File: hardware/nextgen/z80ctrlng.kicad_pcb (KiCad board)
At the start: 4 copper layers, 101.6 x 53.3 mm, 67 parts, among them J1 RCBUS, J11 U254-051T-4BH81-S2S, J3 UDPI, J5 XKTF-0803-0, J6 UEXT, J9 SM04B-SRSS-TB, Q3 BSS138, SW1 RESET, SW2 BANK_EN, SW4 PROG_EN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

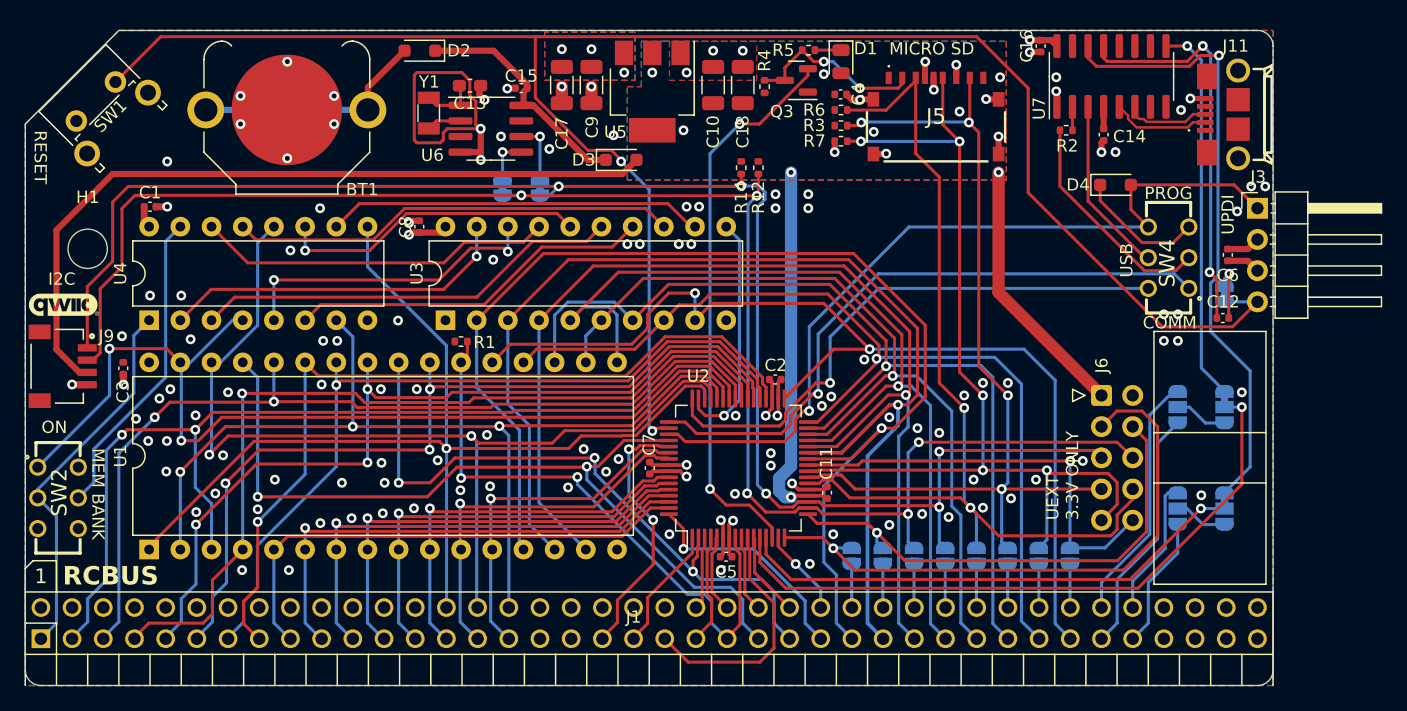
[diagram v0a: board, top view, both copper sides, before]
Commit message: Reorganize hardware directories
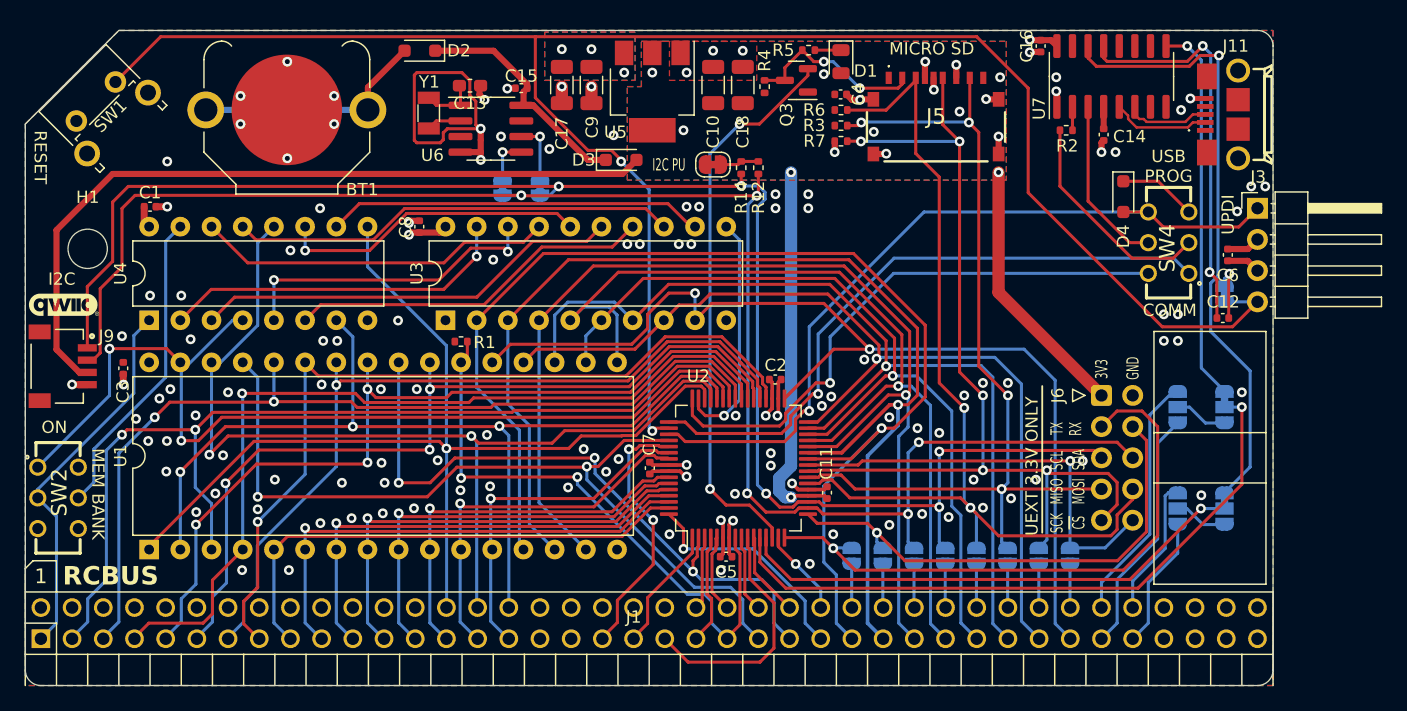
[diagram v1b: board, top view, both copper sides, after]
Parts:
- added JP16: I2C_PU, Jumper:SolderJumper-2_P1.3mm_Bridged_RoundedPad1.0x1.5mm, F.Cu at (183.8, 84.3)
- moved SW4 1.22 mm to (220.9, 90.7)
- moved D4 1.15 mm to (217.2, 86.9), turned to -90 degrees
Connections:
- R12 pad 1: +3.3V -> Net-(JP16-A)
- R14 pad 1: +3.3V -> Net-(JP16-A)
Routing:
- net Net-(D4-K): track 10.4 -> 6.37 mm
- net Net-(JP16-A): track 0.00 -> 3.15 mm
- net UPDI: track 66.2 -> 63.6 mm
- net RXF: track 51.8 -> 52.4 mm
- net /Peripherals/USBRX: track 14.5 -> 14.0 mm
- net TXF: track 46.0 -> 46.5 mm
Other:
- board text added: "3V3"
- board text added: "GND"
- board text added: "I2C PU"
- board text added: "USB PROG"
- board text removed: "PROG"
- board text removed: "USB"

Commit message: Get rid of serial bus links, make banking software controllable
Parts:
- removed JP12: RXB, Jumper:SolderJumper-3_P1.3mm_Open_RoundedPad1.0x1.5mm
- removed JP14: CTS, Jumper:SolderJumper-3_P1.3mm_Bridged12_RoundedPad1.0x1.5mm
- removed JP4: TXB, Jumper:SolderJumper-3_P1.3mm_Open_RoundedPad1.0x1.5mm
- removed JP5: RTS, Jumper:SolderJumper-3_P1.3mm_Bridged12_RoundedPad1.0x1.5mm
- removed SW2: BANK_EN, SamacSys_Parts:JS202011CQN
- added C19: 0.1uf, Capacitor_SMD:C_0402_1005Metric, F.Cu at (130.3, 110.0)
- added U8: 74LVC1G126, Package_TO_SOT_SMD:SOT-353_SC-70-5, F.Cu at (130.5, 112.2)
- U3: value 74HCT574 -> 74HCT573; footprint Package_DIP:DIP-20_W7.62mm -> Package_SO:TSSOP-20_4.4x6.5mm_P0.65mm
- U4: footprint Package_DIP:DIP-16_W7.62mm -> Package_SO:SOIC-16_3.9x9.9mm_P1.27mm
- moved U3 15.2 mm to (176.3, 92.1)
- moved C8 12.4 mm to (172.2, 89.3)
- moved U4 6.01 mm to (141.6, 92.3)
- moved C3 4.87 mm to (137.9, 96.6), turned to 0 degrees
- moved U1 2.23 mm to (137.9, 113.4)
- moved R1 2.22 mm to (163.3, 96.5)
- moved JP15 0.97 mm to (165.9, 85.6)
- moved JP13 0.71 mm to (169.3, 85.6)
- moved JP16 0.34 mm to (183.5, 84.1)
- moved C1 0.31 mm to (137.6, 87.8)
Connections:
- U2 pad 1: /~{Z80RST} -> /~{BUSACK}
- U2 pad 12: TXB -> /~{Z80RST}
- U2 pad 13: RXB -> /~{INT}
- U2 pad 14: ~{SDCS} -> /~{RD}
- U2 pad 2: /~{RD} -> /~{HALT}
- U2 pad 3: /~{BUSACK} -> /A16
- U2 pad 4: /~{INT} -> /A17
- U2 pad 44: /A16 -> /~{BANK}
- U2 pad 45: /A17 -> /BLAT
- U2 pad 46: /A18 -> ~{SDCS}
- U2 pad 47: /BCK -> ~{CTS}
- U2 pad 5: /~{HALT} -> /A18
- U3 pad 11: /BCK -> /BLAT
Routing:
- net /~{BANK}: track 25.5 -> 91.5 mm, vias 0 -> 2
- net TXB: track 53.3 -> 0.00 mm, vias 1 -> 0
- net RXB: track 41.9 -> 0.00 mm, vias 1 -> 0
- net ~{RTS}: track 50.3 -> 12.6 mm
- net ~{CTS}: track 31.1 -> 59.9 mm, vias 1 -> 2
- net ~{RESET}: track 151.4 -> 178.5 mm, vias 2 -> 3
- net /TX2B: track 20.4 -> 0.00 mm
- net /TX1B: track 20.1 -> 0.00 mm
- net /BCK: track 19.5 -> 0.00 mm, vias 1 -> 0
- net /BLAT: track 0.00 -> 18.8 mm, vias 0 -> 2
- net /~{RD}: track 53.8 -> 69.9 mm, vias 3 -> 2
- net /BB18: track 30.8 -> 44.4 mm, vias 0 -> 2
- net ~{SDCS}: track 45.6 -> 32.1 mm
- net /BA17: track 29.1 -> 42.5 mm, vias 0 -> 2
- net /~{Z80RST}: track 10.2 -> 22.4 mm, vias 0 -> 1
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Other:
- board text removed: "BANK MULTIPLEXER 74HCT257"
- board text removed: "BANK REGISTER 74HCT574"
- board text removed: "MEM BANK"
- board text removed: "ON"
- board text removed: "RX1"
- board text removed: "RX2"
- board text removed: "RXB"
- board text removed: "SERIAL CONFIG"
- board text removed: "TX1"
- board text removed: "TX2"
- board text removed: "TXB"
- board text removed: "~{CTS}"
- board text removed: "~{RTS}"
